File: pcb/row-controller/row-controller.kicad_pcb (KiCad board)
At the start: 2 copper layers, 33 parts, among them IC1 INA220BIDGSR, IC2 THVD1420DR, IC3 THVD1420DR, J1 Power, J2 5555140-2, J4 5555140-2, U1 XAIO ESP32-C3, U2 R-78E5.0-0.5

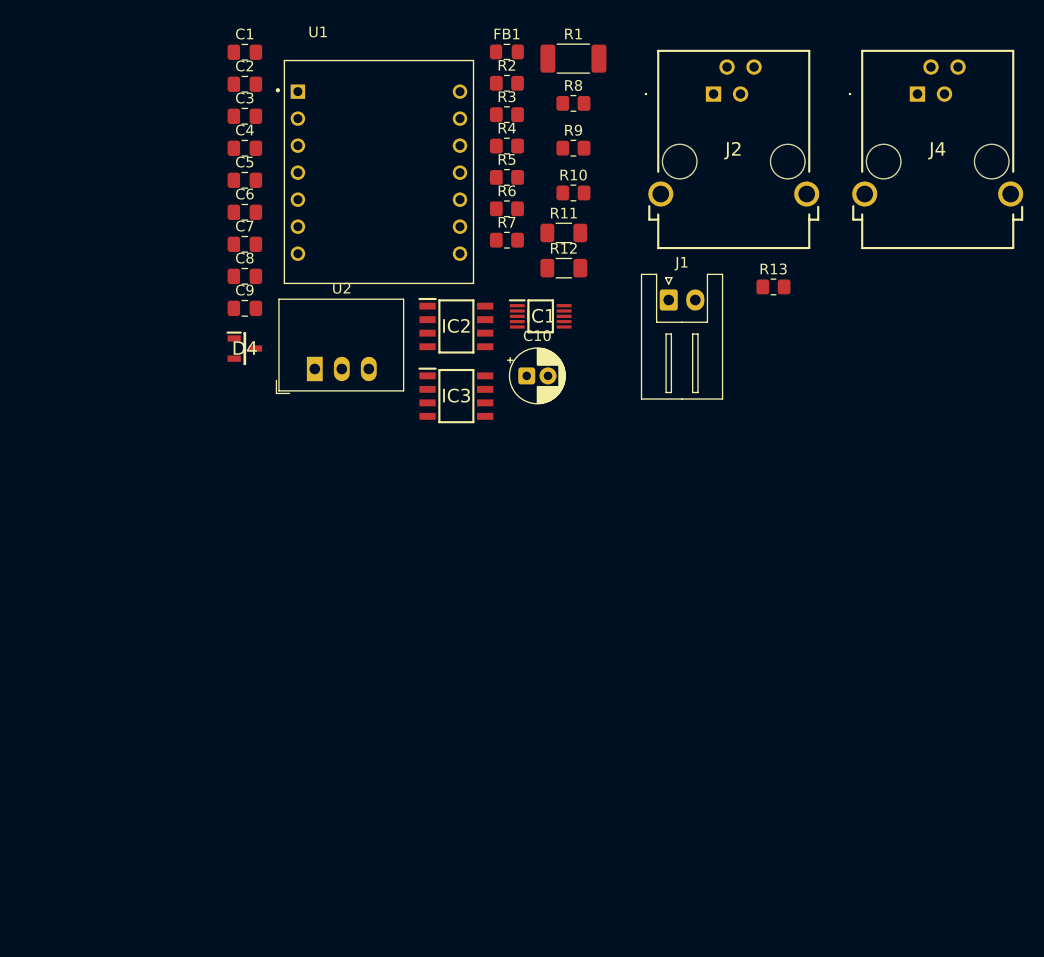
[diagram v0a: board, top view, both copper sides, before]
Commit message: Removed the ferrite bead, updated power symbols.
Not convinced I need the beads, can do some testing to confirm this when I have test boards
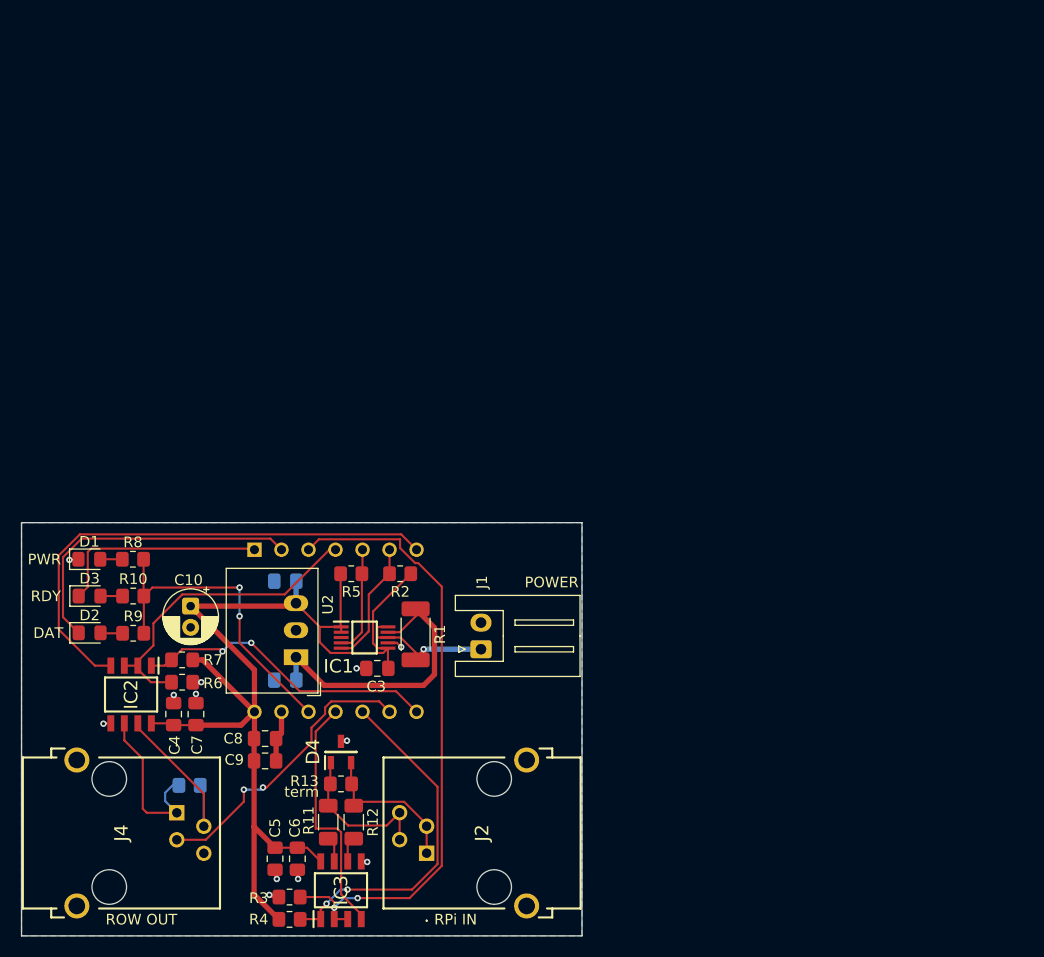
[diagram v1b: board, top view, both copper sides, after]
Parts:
- removed FB1: FerriteBead, Inductor_SMD:L_0805_2012Metric_Pad1.15x1.40mm_HandSolder
- added D1: RED, LED_SMD:LED_0805_2012Metric_Pad1.15x1.40mm_HandSolder, F.Cu at (86.9, 101.2)
- added D2: GREEN, LED_SMD:LED_0805_2012Metric_Pad1.15x1.40mm_HandSolder, F.Cu at (86.9, 108.2)
- added D3: ORANGE, LED_SMD:LED_0805_2012Metric_Pad1.15x1.40mm_HandSolder, F.Cu at (86.9, 104.7)
- added R14: 120ohm, Resistor_SMD:R_0805_2012Metric_Pad1.20x1.40mm_HandSolder, B.Cu at (96.3, 122.5)
- C1, C2, U1: moved to B.Cu
- moved J4 97.0 mm to (95.1, 125.1), turned to -90 degrees
- moved R3 76.3 mm to (105.7, 133.0), turned to 180 degrees
- moved J2 76.3 mm to (118.6, 128.9), turned to 90 degrees
- moved R4 75.5 mm to (105.7, 135.1)
- moved C5 63.9 mm to (104.3, 129.4), turned to -90 degrees
- moved R13 61.9 mm to (110.5, 122.4), turned to 180 degrees
- moved R9 61.6 mm to (91.0, 108.2), turned to 180 degrees
- moved C6 61.0 mm to (106.4, 129.4), turned to -90 degrees
- moved R11 59.7 mm to (109.3, 126.0), turned to 90 degrees
- moved R8 59.6 mm to (91.0, 101.2), turned to 180 degrees
- moved C1 59.2 mm to (105.3, 112.6), turned to 180 degrees
- moved R1 56.1 mm to (117.6, 108.3), turned to 90 degrees
- moved R10 56.1 mm to (91.0, 104.7), turned to 180 degrees
- moved R12 55.7 mm to (111.7, 126.0), turned to 90 degrees
- moved R6 54.0 mm to (95.6, 112.8)
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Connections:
- C8 pad 1: +VDC -> +5V
- C9 pad 1: +VDC -> +5V
- U1 pad 14: +VDC -> +5V
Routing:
- net +5V: track 0.00 -> 101.4 mm
- net /PI-XDIR: track 0.00 -> 59.5 mm, vias 0 -> 2
- net /ROW-TxD: track 0.00 -> 48.3 mm
- net /PI-RxD: track 0.00 -> 32.8 mm, vias 0 -> 2
- net +3V3: track 0.00 -> 30.7 mm, vias 0 -> 2
- net /ROW-XDIR: track 0.00 -> 29.9 mm
- net /LED-DATA: track 0.00 -> 29.4 mm
- net /ROW-RxD: track 0.00 -> 28.7 mm, vias 0 -> 2
- net /ROW-SENSE: track 0.00 -> 27.6 mm, vias 0 -> 2
- net /Vrow: track 0.00 -> 27.5 mm
- net /PI-TxD: track 0.00 -> 23.2 mm
- net /LED-RDY: track 0.00 -> 20.3 mm
- net /ROW-TRCV-B: track 0.00 -> 16.2 mm
- net /ROW-TRCV-A: track 0.00 -> 16.0 mm
- net GND: track 0.00 -> 15.6 mm, vias 0 -> 12
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- added copper zone on B.Cu, net GND
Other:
- board outline added: 52.7 x 38.9 mm
- board text added: "12V"
- board text added: "2025-10-29 v1.0"
- board text added: "5V"
- board text added: "DAT"
- board text added: "GND"
- board text added: "POWER"
- board text added: "PWR"
- board text added: "RDY"
- board text added: "ROW OUT"
- board text added: "RPi IN"
- board text added: "Row Controller"
- board text added: "SENSE"
- board text added: "TRCV-A"
- board text added: "TRCV-B"
- board text added: "[BOARD_COST] 2.067in x 1.506in | 3.113 in^2 | $15.56"
- board text added: "term"

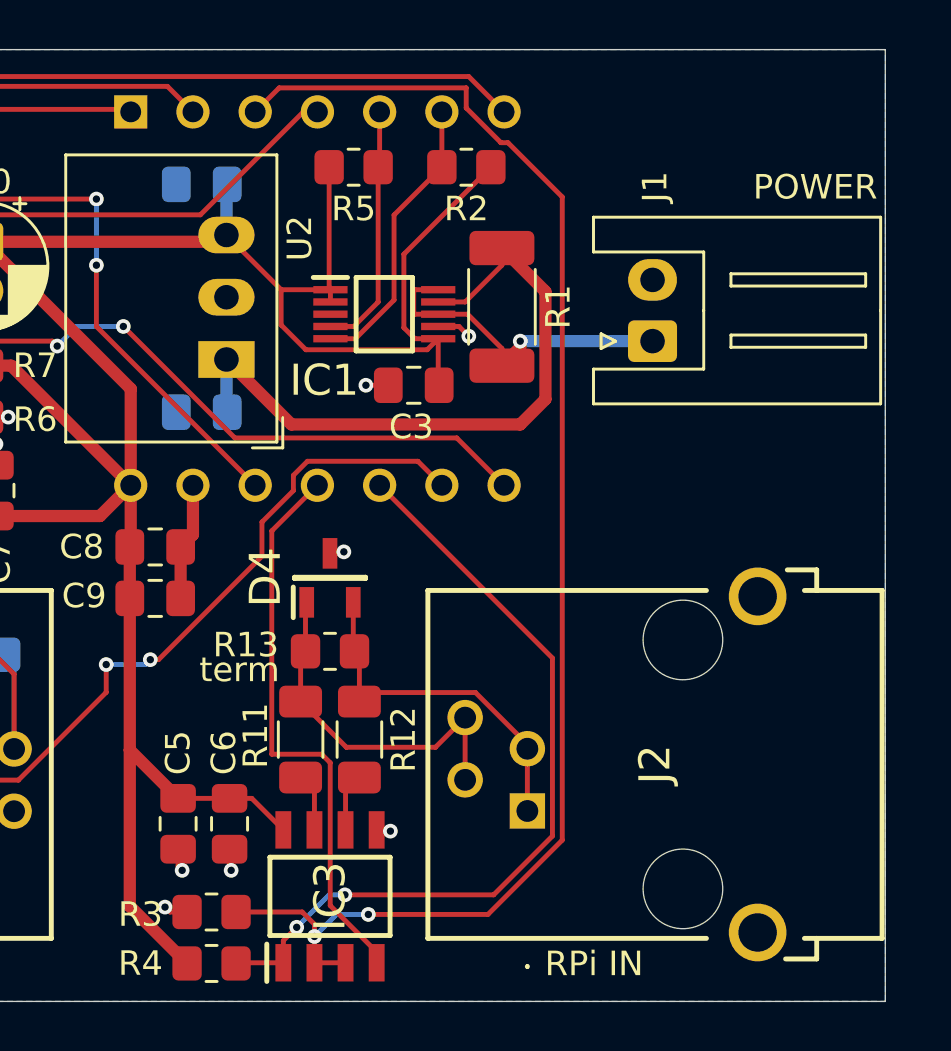
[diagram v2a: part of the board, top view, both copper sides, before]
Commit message: Row controller with two power jacks; in from main power, out for row power
This is necessary to actually measure the power sent to the row
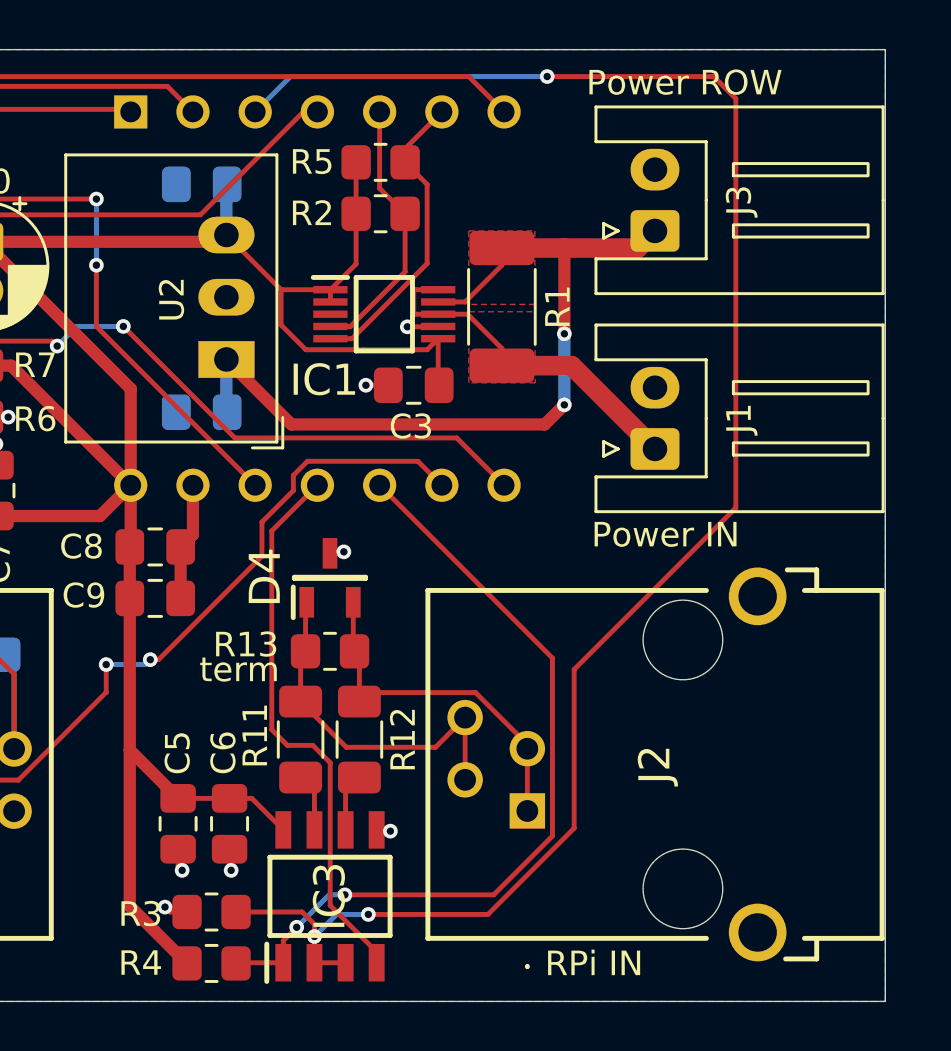
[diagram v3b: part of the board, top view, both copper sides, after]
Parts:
- added J3: Power Row, Connector_JST:JST_XH_S2B-XH-A_1x02_P2.50mm_Horizontal, F.Cu at (123.8, 105.2)
- J1: value Power -> Power In
- moved J1 4.40 mm to (123.8, 114.1)
- moved R5 3.51 mm to (112.6, 102.4), turned to 0 degrees
- moved R2 2.20 mm to (112.6, 104.5)
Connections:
- net /Vrow renamed Vrow
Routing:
- net /PI-XDIR: track 59.5 -> 71.8 mm, vias 2 -> 3
- net +5V: track 101.4 -> 92.5 mm
- net Vrow: track 27.5 -> 34.2 mm, vias 0 -> 2
- net +12V: track 13.5 -> 14.5 mm, vias 1 -> 0
- net /SDA: track 10.1 -> 10.9 mm
- net /SCL: track 11.7 -> 12.4 mm
- net /PI-TxD: track 23.2 -> 22.6 mm
- added copper zone on F.Cu, net +12V
- added copper zone on F.Cu, net Vrow
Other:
- board text added: "2025-10-29 v1.1"
- board text added: "Power IN"
- board text added: "Power ROW"
- board text removed: "2025-10-29 v1.0"
- board text removed: "POWER"
